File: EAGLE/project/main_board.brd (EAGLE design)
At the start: 76.2 x 100 mm, 5 parts, among them U1 RASPBERRY_PI_4B_4GB, U2 2472, X1 MKDSN1,5/3-5,08, X2 MKDSN1,5/3-5,08

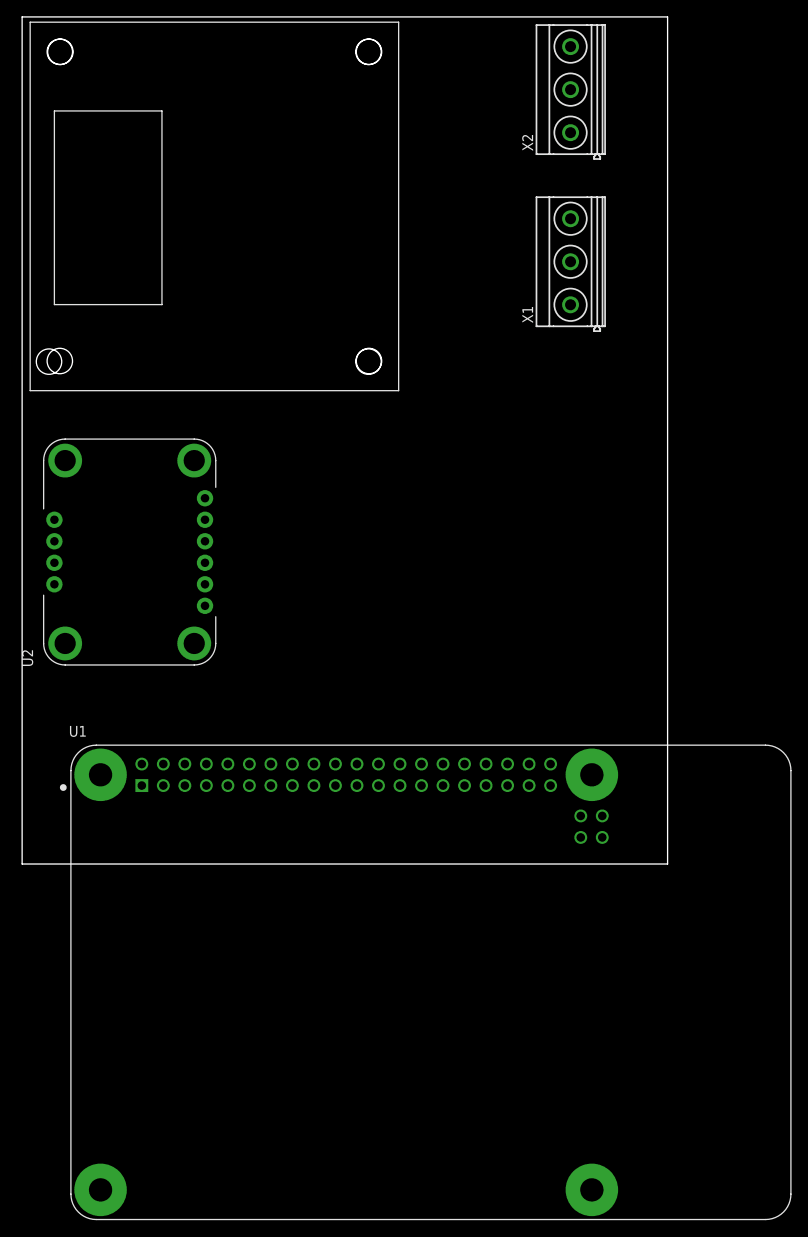
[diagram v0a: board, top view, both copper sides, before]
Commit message: design main board PCB by EAGLE
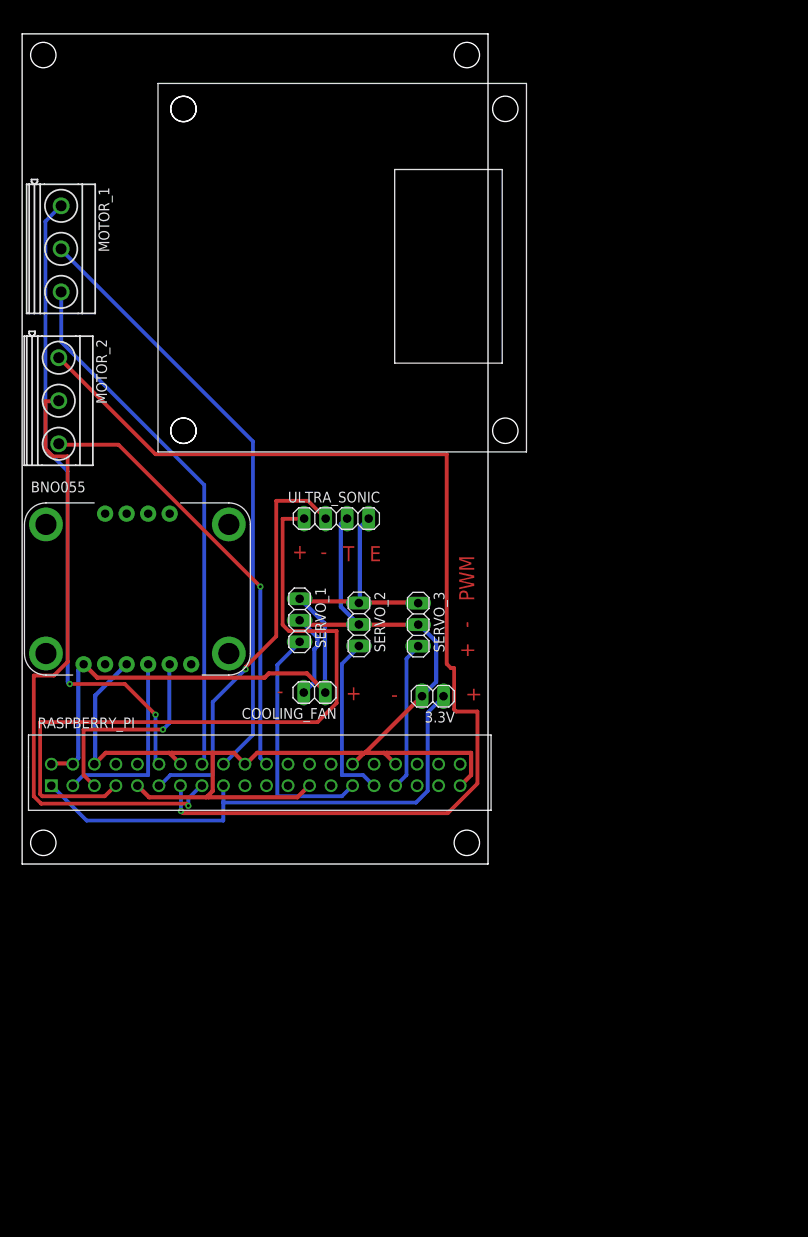
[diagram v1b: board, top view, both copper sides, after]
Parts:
- removed U1: RASPBERRY_PI_4B_4GB, RASPBERRY_PI_4B_4GB:MODULE_RASPBERRY_PI_4B_4GB
- removed U2: 2472, BNO055_IMU:MODULE_2472
- removed X1, X2: MKDSN1,5/3-5,08, con-phoenix-508:MKDSN1,5/3-5,08
- added 3.3V, COOLING_FAN: (no value), pinhead:1X02
- added BNO055: 2472, BNO055_IMU:MODULE_2472
- added MOTOR_1, MOTOR_2: MKDSN1,5/3-5,08, con-phoenix-508:MKDSN1,5/3-5,08
- added RASPBERRY_PI: RASPBERRY_PI_4B_4GB, RASPBERRY_PI_4B_4GB:MODULE_RASPBERRY_PI_4B_4GB
- added SERVO_1, SERVO_2, SERVO_3: (no value), pinhead:1X03
- added ULTRA_SONIC: (no value), pinhead:1X04
- moved L298N1 46.1 mm to (16.0, 92.2), turned to 270 degrees
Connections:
- removed net 3V3: U1.1, U1.17
- removed net N$1: U1.2, U1.4, U2.1
- removed net N$10: U1.22, X2.3
- removed net N$2: U1.14, U1.20, U1.25, U1.30, U1.34, U1.39, U1.6, U1.9, U2.3
- removed net N$3: U1.3, U2.4
- removed net N$4: U1.5, U2.5
- removed net N$5: U1.12, X1.1
- removed net N$6: U1.18, X1.2
- removed net N$7: U1.16, X1.3
- removed net N$8: U1.13, X2.1
- removed net N$9: U1.15, X2.2
- removed net SHIELD: U1.S1, U1.S2, U1.S3, U1.S4
- new net 3.3V: 3.3V.1, RASPBERRY_PI.1, RASPBERRY_PI.17
- new net 5V: BNO055.1, COOLING_FAN.1, RASPBERRY_PI.2, RASPBERRY_PI.4, SERVO_1.1, SERVO_2.1, SERVO_3.1, ULTRA_SONIC.1
- new net BNO055_SCL: BNO055.5, RASPBERRY_PI.5
- new net BNO055_SDA: BNO055.4, RASPBERRY_PI.3
- new net ENA: MOTOR_1.1, RASPBERRY_PI.12
- new net ENB: MOTOR_2.3, RASPBERRY_PI.22
- new net GND: 3.3V.2, BNO055.3, COOLING_FAN.2, RASPBERRY_PI.14, RASPBERRY_PI.20, RASPBERRY_PI.25, RASPBERRY_PI.30, RASPBERRY_PI.34, RASPBERRY_PI.39, RASPBERRY_PI.6, RASPBERRY_PI.9, SERVO_1.2, SERVO_2.2, SERVO_3.2, ULTRA_SONIC.2
- new net IN1: MOTOR_1.2, RASPBERRY_PI.18
- new net IN2: MOTOR_1.3, RASPBERRY_PI.16
- new net IN3: MOTOR_2.1, RASPBERRY_PI.13
- new net IN4: MOTOR_2.2, RASPBERRY_PI.15
- new net PWM_SERVO_1: RASPBERRY_PI.29, SERVO_1.3
- new net PWM_SERVO_2: RASPBERRY_PI.31, SERVO_2.3
- new net PWM_SERVO_3: RASPBERRY_PI.33, SERVO_3.3
- new net ULTRA_SONIC_1: RASPBERRY_PI.7, ULTRA_SONIC.4
- new net ULTRA_SONIC_2: RASPBERRY_PI.11, ULTRA_SONIC.3
- net 3VO: now also BNO055.2; no longer U2.2
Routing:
- net GND: track 0.00 -> 154.0 mm
- net IN3: track 0.00 -> 132.2 mm, vias 0 -> 1
- net ULTRA_SONIC_1: track 0.00 -> 84.2 mm
- net 5V: track 0.00 -> 82.5 mm
- net ENA: track 0.00 -> 76.0 mm, vias 0 -> 2
- net IN4: track 0.00 -> 75.2 mm, vias 0 -> 1
- net IN1: track 0.00 -> 71.7 mm
- net IN2: track 0.00 -> 62.9 mm
- net 3.3V: track 0.00 -> 62.8 mm
- net ENB: track 0.00 -> 52.1 mm, vias 0 -> 1
- net ULTRA_SONIC_2: track 0.00 -> 49.1 mm, vias 0 -> 1
- net PWM_SERVO_1: track 0.00 -> 28.7 mm
- net BNO055_SCL: track 0.00 -> 24.6 mm, vias 0 -> 1
- net BNO055_SDA: track 0.00 -> 22.5 mm
- net PWM_SERVO_2: track 0.00 -> 20.4 mm
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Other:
- board size 76.2 x 100 mm -> 55 x 98 mm
- board text added: "+"
- board text added: "-"
- board text added: "E"
- board text added: "PWM"
- board text added: "T"
